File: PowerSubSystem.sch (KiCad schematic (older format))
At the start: 4 parts

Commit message: Added PSU_ prepend to PSU specific global labels in the schematic
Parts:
- C1, C2: symbol pspice:CAP -> BeagleBone-Black-Cape-rescue:CAP-pspice
- L1: symbol pspice:INDUCTOR -> BeagleBone-Black-Cape-rescue:INDUCTOR-pspice
- gave numbers to parts that had none: 1
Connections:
- net labels added: PSU_3V3Out+, PSU_3V3Out-, PSU_5VIn+, PSU_5VIn-
- net labels removed: 3V3Out+, 3V3Out-, 5VIn+, 5VIn-
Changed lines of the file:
@@
 $EndDescr
 $Comp
-L pwr_BeagleBone:TR05S3V3 U?
+L pwr_BeagleBone:TR05S3V3 U1
 U 1 1 610F8923
 P 7000 2950
-F 0 "U?" H 7778 2796 50  0000 L CNN
+F 0 "U1" H 7778 2796 50  0000 L CNN
 F 1 "TR05S3V3" H 7778 2705 50  0000 L CNN
 F 2 "" H 7000 2950 50  0001 C CNN
@@
 $EndComp
 $Comp
-L pspice:INDUCTOR L1
+L BeagleBone-Black-Cape-rescue:INDUCTOR-pspice L1
 U 1 1 610F8FF3
 P 5950 3050
@@
 $EndComp
 $Comp
-L pspice:CAP C1
+L BeagleBone-Black-Cape-rescue:CAP-pspice C1
 U 1 1 610F97C7
 P 5550 3450
@@
 $EndComp
 $Comp
-L pspice:CAP C2
+L BeagleBone-Black-Cape-rescue:CAP-pspice C2
 U 1 1 610FA119
 P 6350 3450
@@
 Connection ~ 5550 3850
 Text GLabel 7400 3750 2    50   Output ~ 0
-3V3Out+
+PSU_3V3Out+
 Text GLabel 7400 3850 2    50   Output ~ 0
-3V3Out-
+PSU_3V3Out-
 Text GLabel 5400 3050 0    50   Input ~ 0
-5VIn+
+PSU_5VIn+
 Text GLabel 5400 3850 0    50   Input ~ 0
-5VIn-
+PSU_5VIn-
 $Comp
-L power:GND #PWR?
+L BeagleBone-Black-Cape-rescue:GND-power #PWR?
 U 1 1 611018D2
 P 6350 3950

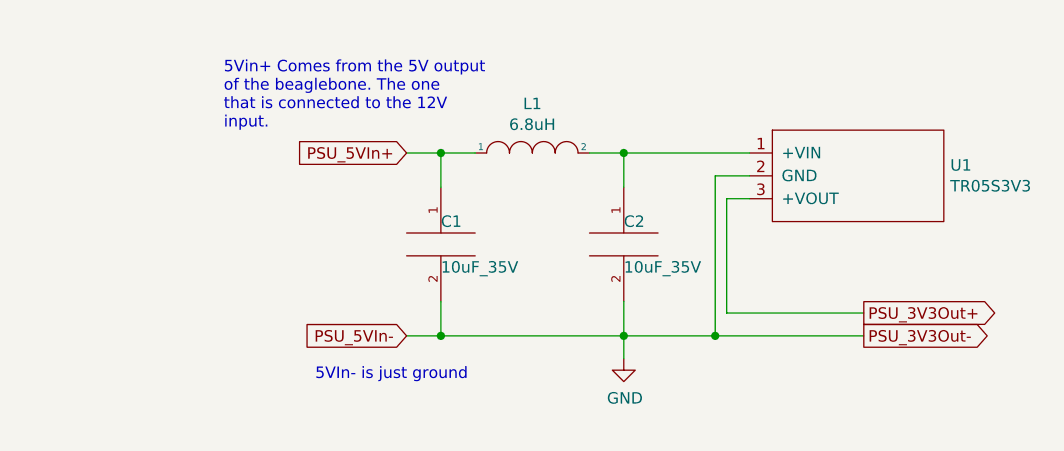
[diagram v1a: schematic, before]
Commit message: Replaced old PSU circuit with the new one
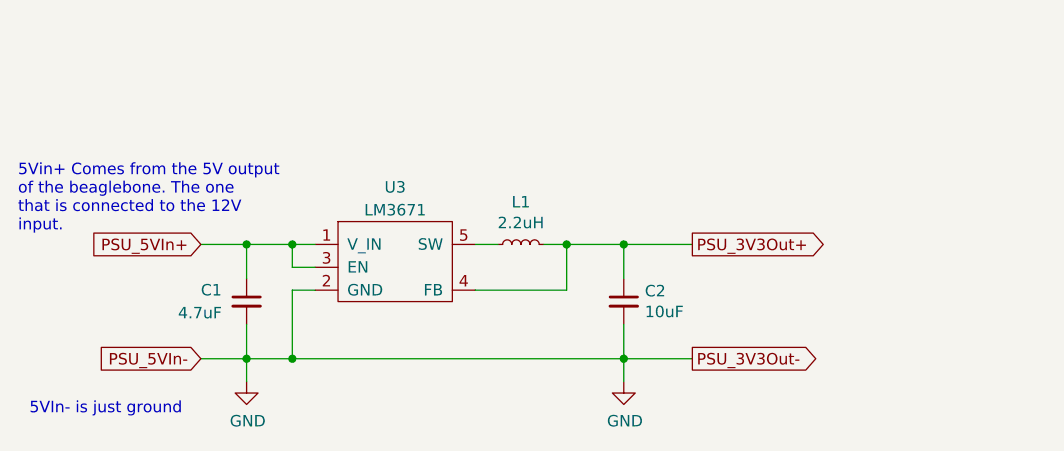
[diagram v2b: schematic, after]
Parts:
- removed C1, C2: 10uF_35V, symbol BeagleBone-Black-Cape-rescue:CAP-pspice
- removed L1: 6.8uH, symbol BeagleBone-Black-Cape-rescue:INDUCTOR-pspice
- removed U1: TR05S3V3, symbol pwr_BeagleBone:TR05S3V3
- added C1: 4.7uF, Capacitor_SMD:C_0805_2012Metric, symbol Device:C_Small
- added C2: 10uF, Capacitor_SMD:C_0805_2012Metric, symbol Device:C_Small
- added L1: 2.2uH, Inductor_SMD:L_1210_3225Metric, symbol Device:L_Small
- added U3: LM3671, Package_TO_SOT_SMD:SOT-23-5, symbol pwr_BeagleBone:LM3671
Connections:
- net GND: now also C1.2, C2.2, U3.2 (GND)
- net PSU_3V3Out+: now also C2.1, L1.2, U3.4 (FB)
- net PSU_5VIn+: now also C1.1, U3.1 (V_IN), U3.3 (EN)
- new net: L1.1, U3.5 (SW)
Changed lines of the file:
@@
 Comment4 ""
 $EndDescr
+Text Notes 3750 4200 0    50   ~ 0
+5VIn- is just ground
+Text Notes 3700 3400 0    50   ~ 0
+5Vin+ Comes from the 5V output \nof the beaglebone. The one \nthat is connected to the 12V \ninput.
 $Comp
-L pwr_BeagleBone:TR05S3V3 U1
-U 1 1 610F8923
-P 7000 2950
-F 0 "U1" H 7778 2796 50  0000 L CNN
-F 1 "TR05S3V3" H 7778 2705 50  0000 L CNN
-F 2 "" H 7000 2950 50  0001 C CNN
-F 3 "" H 7000 2950 50  0001 C CNN
-	1    7000 2950
+L pwr_BeagleBone:LM3671 U3
+U 1 1 613D6B2B
+P 5350 3300
+F 0 "U3" H 5350 3400 50  0000 C CNN
+F 1 "LM3671" H 5350 3300 50  0000 C CNN
+F 2 "Package_TO_SOT_SMD:SOT-23-5" H 5350 3300 50  0001 C CNN
+F 3 "https://www.ti.com/lit/ds/symlink/lm3671.pdf?HQS=dis-mous-null-mousermode-dsf-pf-null-wwe&ts=1631307057229&ref_url=https%253A%252F%252Fwww.mouser.com%252F" H 5350 3300 50  0001 C CNN
+	1    5350 3300
+	1    0    0    -1
+$EndComp
+Text GLabel 4500 3450 0    50   Input ~ 0
+PSU_5VIn+
+$Comp
+L Device:C_Small C1
+U 1 1 613D8B5E
+P 4700 3700
+F 0 "C1" H 4500 3750 50  0000 L CNN
+F 1 "4.7uF" H 4400 3650 50  0000 L CNN
+F 2 "Capacitor_SMD:C_0805_2012Metric" H 4700 3700 50  0001 C CNN
+F 3 "https://www.mouser.com/datasheet/2/396/mlcc02_e-1307760.pdf" H 4700 3700 50  0001 C CNN
+	1    4700 3700
+	1    0    0    -1
+$EndComp
+Wire Wire Line
+	4500 3450 4700 3450
+Wire Wire Line
+	4700 3600 4700 3450
+Wire Wire Line
+	4700 3800 4700 3950
+Text GLabel 4500 3950 0    50   Input ~ 0
+PSU_5VIn-
+Wire Wire Line
+	4500 3950 4700 3950
+Connection ~ 4700 3950
+Wire Wire Line
+	5000 3550 4900 3550
+Wire Wire Line
+	4900 3550 4900 3450
+Wire Wire Line
+	4900 3450 5000 3450
+Wire Wire Line
+	5000 3650 4900 3650
+Wire Wire Line
+	4900 3650 4900 3950
+$Comp
+L Device:L_Small L1
+U 1 1 613E2221
+P 5900 3450
+F 0 "L1" V 6085 3450 50  0000 C CNN
+F 1 "2.2uH" V 5994 3450 50  0000 C CNN
+F 2 "Inductor_SMD:L_1210_3225Metric" H 5900 3450 50  0001 C CNN
+F 3 "~https://www.mouser.com/datasheet/2/54/cm322522-777598.pdf" H 5900 3450 50  0001 C CNN
+	1    5900 3450
+	0    -1   -1   0
+$EndComp
+Wire Wire Line
+	5700 3450 5800 3450
+Wire Wire Line
+	6100 3650 6100 3450
+$Comp
+L power:GND #PWR0102
+U 1 1 613E4C24
+P 4700 4050
+F 0 "#PWR0102" H 4700 3800 50  0001 C CNN
+F 1 "GND" H 4705 3877 50  0000 C CNN
+F 2 "" H 4700 4050 50  0001 C CNN
+F 3 "" H 4700 4050 50  0001 C CNN
+	1    4700 4050
+	1    0    0    -1
+$EndComp
+Wire Wire Line
+	4700 4050 4700 3950
+$Comp
+L Device:C_Small C2
+U 1 1 613E66FD
+P 6350 3700
+F 0 "C2" H 6442 3746 50  0000 L CNN
+F 1 "10uF" H 6442 3655 50  0000 L CNN
+F 2 "Capacitor_SMD:C_0805_2012Metric" H 6350 3700 50  0001 C CNN
+F 3 "https://www.mouser.com/datasheet/2/396/mlcc02_e-1307760.pdf" H 6350 3700 50  0001 C CNN
+	1    6350 3700
 	1    0    0    -1
 $EndComp
 $Comp
-L BeagleBone-Black-Cape-rescue:INDUCTOR-pspice L1
-U 1 1 610F8FF3
-P 5950 3050
-F 0 "L1" H 5950 3265 50  0000 C CNN
-F 1 "6.8uH" H 5950 3174 50  0000 C CNN
-F 2 "" H 5950 3050 50  0001 C CNN
-F 3 "~" H 5950 3050 50  0001 C CNN
-	1    5950 3050
+L power:GND #PWR0109
+U 1 1 613EB575
+P 6350 4050
+F 0 "#PWR0109" H 6350 3800 50  0001 C CNN
+F 1 "GND" H 6355 3877 50  0000 C CNN
+F 2 "" H 6350 4050 50  0001 C CNN
+F 3 "" H 6350 4050 50  0001 C CNN
+	1    6350 4050
 	1    0    0    -1
 $EndComp
-$Comp
-L BeagleBone-Black-Cape-rescue:CAP-pspice C1
-U 1 1 610F97C7
-P 5550 3450
-F 0 "C1" H 5550 3550 50  0000 L CNN
-F 1 "10uF_35V" H 5550 3350 50  0000 L CNN
-F 2 "" H 5550 3450 50  0001 C CNN
-F 3 "~" H 5550 3450 50  0001 C CNN
-	1    5550 3450
-	1    0    0    -1
-$EndComp
-$Comp
-L BeagleBone-Black-Cape-rescue:CAP-pspice C2
-U 1 1 610FA119
-P 6350 3450
-F 0 "C2" H 6350 3550 50  0000 L CNN
-F 1 "10uF_35V" H 6350 3350 50  0000 L CNN
-F 2 "" H 6350 3450 50  0001 C CNN
-F 3 "~" H 6350 3450 50  0001 C CNN
-	1    6350 3450
-	1    0    0    -1
-$EndComp
+Text GLabel 6650 3450 2    50   Output ~ 0
+PSU_3V3Out+
 Wire Wire Line
-	6200 3050 6350 3050
+	6350 3450 6350 3600
 Wire Wire Line
-	6350 3050 6350 3200
+	6100 3450 6350 3450
 Wire Wire Line
-	5550 3200 5550 3050
+	6350 3450 6650 3450
+Connection ~ 6350 3450
+Text GLabel 6650 3950 2    50   Output ~ 0
+PSU_3V3Out-
 Wire Wire Line
-	5550 3050 5700 3050
+	6650 3950 6350 3950
 Wire Wire Line
-	6350 3050 6900 3050
-Connection ~ 6350 3050
+	6350 3950 6350 3800
 Wire Wire Line
-	6750 3850 6750 3150
+	6350 4050 6350 3950
+Connection ~ 6350 3950
 Wire Wire Line
-	6750 3150 6900 3150
+	4700 3950 4900 3950
 Wire Wire Line
-	6900 3250 6800 3250
+	4900 3450 4700 3450
+Connection ~ 4900 3450
+Connection ~ 4700 3450
 Wire Wire Line
-	6800 3250 6800 3750
+	6000 3450 6100 3450
+Connection ~ 6100 3450
 Wire Wire Line
-	6800 3750 7400 3750
+	5700 3650 6100 3650
 Wire Wire Line
-	6750 3850 7400 3850
-Wire Wire Line
-	5550 3700 5550 3850
-Wire Wire Line
-	5550 3850 6350 3850
-Wire Wire Line
-	6350 3700 6350 3850
-Connection ~ 6350 3850
-Wire Wire Line
-	6350 3850 6750 3850
-Connection ~ 6750 3850
-Wire Wire Line
-	5400 3050 5550 3050
-Connection ~ 5550 3050
-Wire Wire Line
-	5550 3850 5400 3850
-Connection ~ 5550 3850
-Text GLabel 7400 3750 2    50   Output ~ 0
-PSU_3V3Out+
-Text GLabel 7400 3850 2    50   Output ~ 0
-PSU_3V3Out-
-Text GLabel 5400 3050 0    50   Input ~ 0
-PSU_5VIn+
-Text GLabel 5400 3850 0    50   Input ~ 0
-PSU_5VIn-
-$Comp
-L BeagleBone-Black-Cape-rescue:GND-power #PWR?
-U 1 1 611018D2
-P 6350 3950
-F 0 "#PWR?" H 6350 3700 50  0001 C CNN
-F 1 "GND" H 6355 3777 50  0000 C CNN
-F 2 "" H 6350 3950 50  0001 C CNN
-F 3 "" H 6350 3950 50  0001 C CNN
-	1    6350 3950
-	1    0    0    -1
-$EndComp
-Wire Wire Line
-	6350 3950 6350 3850
-Text Notes 5000 4050 0    50   ~ 0
-5VIn- is just ground
-Text Notes 4600 2950 0    50   ~ 0
-5Vin+ Comes from the 5V output \nof the beaglebone. The one \nthat is connected to the 12V \ninput.
+	4900 3950 6350 3950
+Connection ~ 4900 3950
 $EndSCHEMATC

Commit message: PSU footprint validation done. Also updated reference values for L and C for that subsystem.
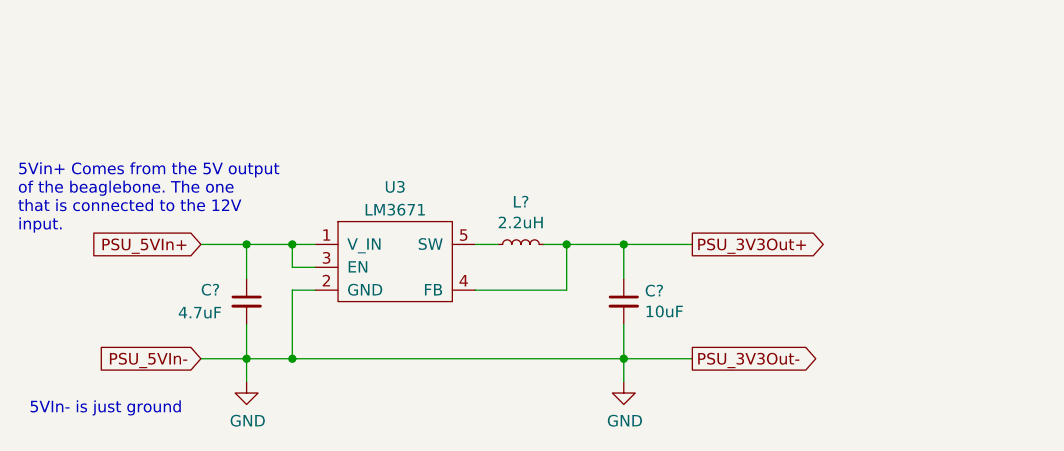
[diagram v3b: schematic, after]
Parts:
- renumbered C1 to C?, C2 to C?, L1 to L?
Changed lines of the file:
@@
 PSU_5VIn+
 $Comp
-L Device:C_Small C1
+L Device:C_Small C?
 U 1 1 613D8B5E
 P 4700 3700
-F 0 "C1" H 4500 3750 50  0000 L CNN
+F 0 "C?" H 4500 3750 50  0000 L CNN
 F 1 "4.7uF" H 4400 3650 50  0000 L CNN
 F 2 "Capacitor_SMD:C_0805_2012Metric" H 4700 3700 50  0001 C CNN
@@
 	4900 3650 4900 3950
 $Comp
-L Device:L_Small L1
+L Device:L_Small L?
 U 1 1 613E2221
 P 5900 3450
-F 0 "L1" V 6085 3450 50  0000 C CNN
+F 0 "L?" V 6085 3450 50  0000 C CNN
 F 1 "2.2uH" V 5994 3450 50  0000 C CNN
 F 2 "Inductor_SMD:L_1210_3225Metric" H 5900 3450 50  0001 C CNN
@@
 	4700 4050 4700 3950
 $Comp
-L Device:C_Small C2
+L Device:C_Small C?
 U 1 1 613E66FD
 P 6350 3700
-F 0 "C2" H 6442 3746 50  0000 L CNN
+F 0 "C?" H 6442 3746 50  0000 L CNN
 F 1 "10uF" H 6442 3655 50  0000 L CNN
 F 2 "Capacitor_SMD:C_0805_2012Metric" H 6350 3700 50  0001 C CNN
